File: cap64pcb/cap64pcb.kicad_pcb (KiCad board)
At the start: 2 copper layers, 91.6 x 8 mm, 29 parts, among them J1 SM05B_SURS_TF, Q1 BSS138, Q2 BSS138, U1 MPR121QR2, U2 SPX3819M5-L-3-3

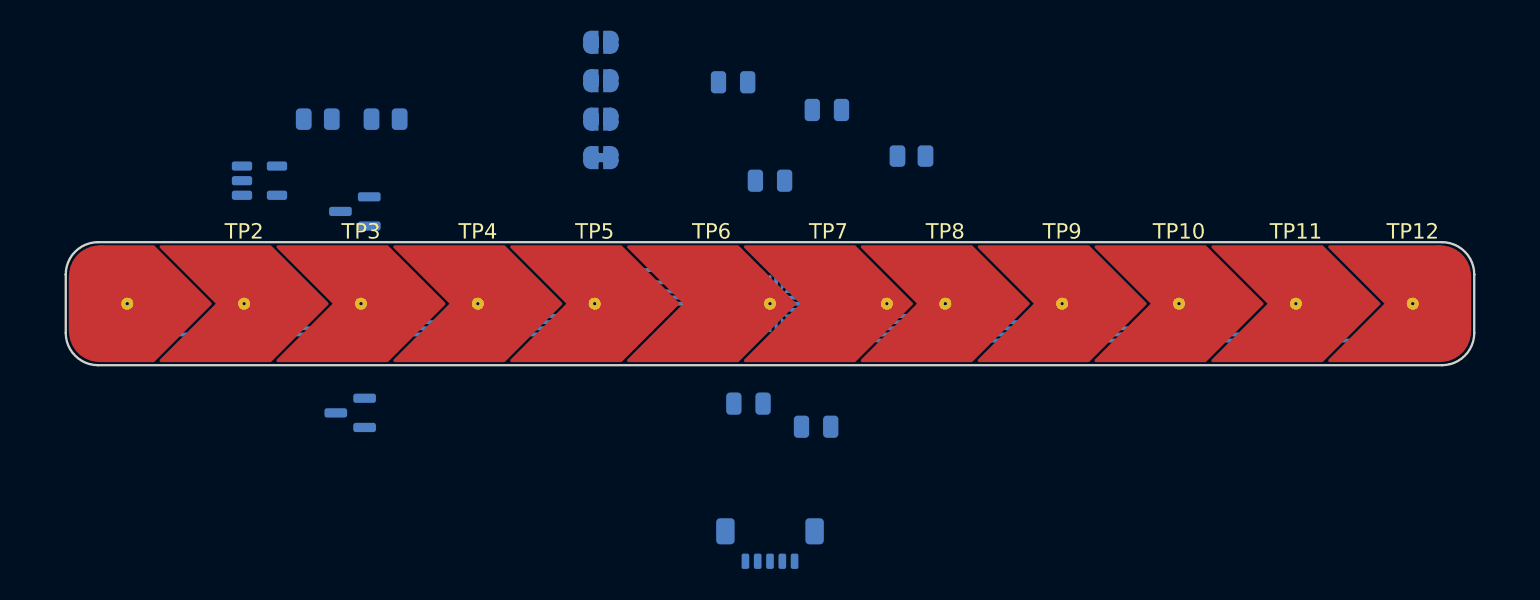
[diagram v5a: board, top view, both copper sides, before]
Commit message: shifted PTH up on touch pads
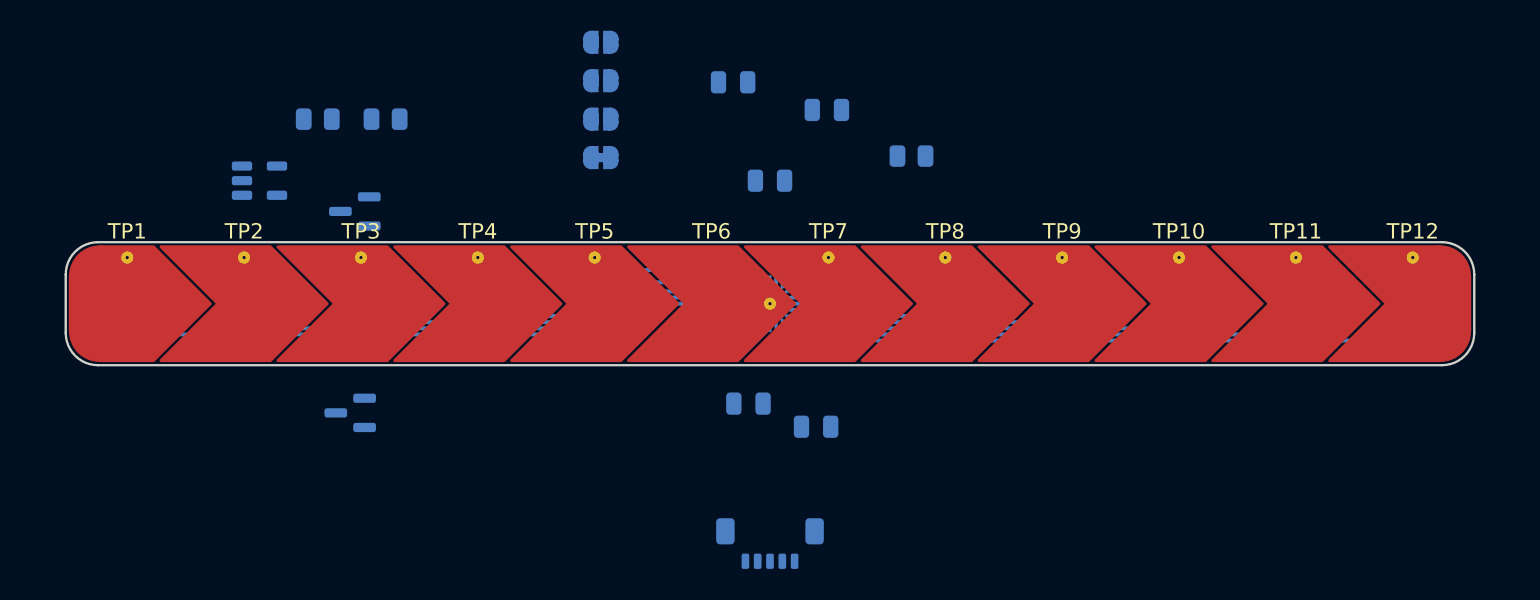
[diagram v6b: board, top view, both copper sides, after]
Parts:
- TP1: footprint cap_pads:CAPPAD_7.6x7.6_Chevron_1 -> cap_pads:CAPPAD_7.6x7.6_Chevron_1_TopPTH
- TP10, TP11, TP2, TP3, TP4, TP5, TP8, TP9: footprint cap_pads:CAPPAD_7.6x7.6_Chevron_2 -> cap_pads:CAPPAD_7.6x7.6_Chevron_2_TopPTH
- TP12: footprint cap_pads:CAPPAD_7.6x7.6_Chevron_3 -> cap_pads:CAPPAD_7.6x7.6_Chevron_3_TopPTH
- TP7: footprint cap_pads:CAPPAD_7.6x7.6_Chevron_2_shifted -> cap_pads:CAPPAD_7.6x7.6_Chevron_2_TopPTH

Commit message: rerouted pads
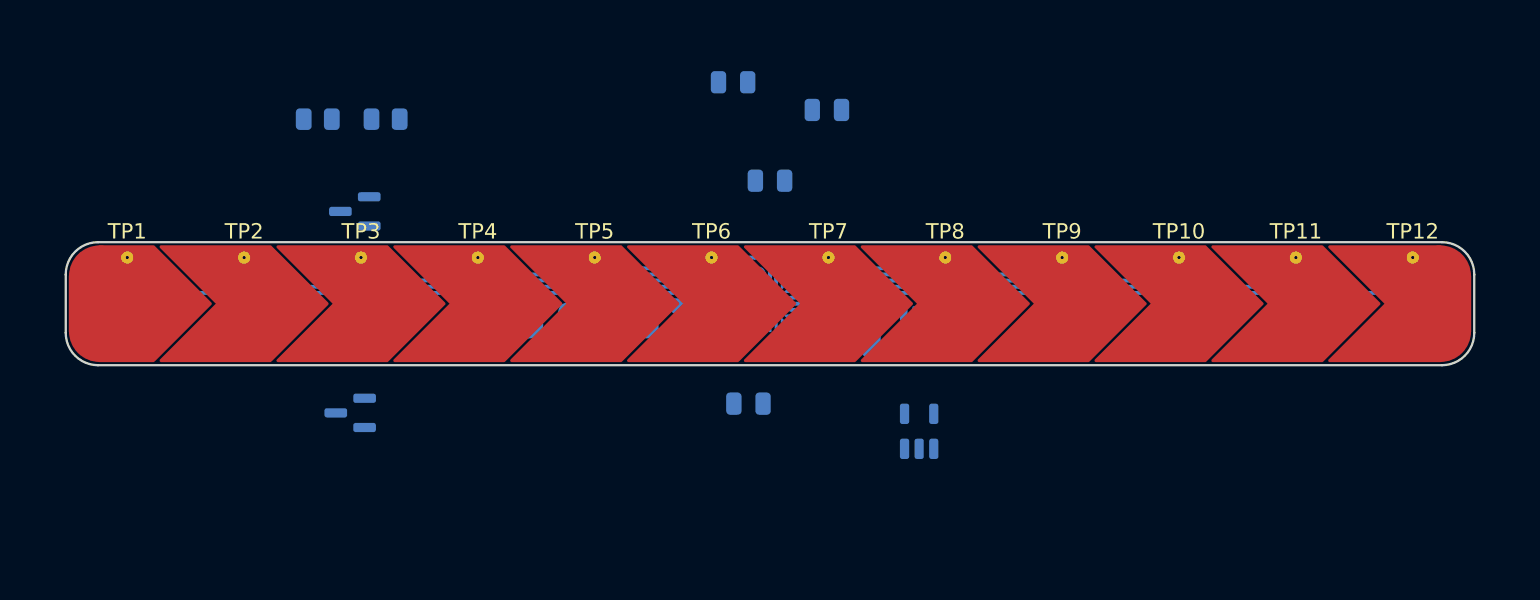
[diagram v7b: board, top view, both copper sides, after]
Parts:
- TP6: footprint cap_pads:CAPPAD_7.6x7.6_Chevron_2_shifted -> cap_pads:CAPPAD_7.6x7.6_Chevron_2_TopPTH
- moved U2 45.9 mm to (89.7, 53.3), turned to 90 degrees
- moved JP1 18.1 mm to (69.5, 46.1), turned to 90 degrees
- moved R1 16.8 mm to (76.3, 46.1), turned to -90 degrees
- moved J1 16.8 mm to (89.5, 46.8), turned to 180 degrees
- moved JP2 15.7 mm to (67.0, 46.1), turned to 90 degrees
- moved JP3 13.9 mm to (64.5, 46.1), turned to 90 degrees
- moved C5 11.1 mm to (74.3, 46.1), turned to 90 degrees
- moved JP4 11.0 mm to (72.0, 46.1), turned to -90 degrees
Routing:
- net Net-(U1-Pad14): track 8.60 -> 4.54 mm
- net Net-(U1-Pad13): track 1.39 -> 4.94 mm
- net Net-(U1-Pad7): track 0.00 -> 2.40 mm
- net Net-(U1-Pad19): track 42.0 -> 43.2 mm
- net Net-(U1-Pad8): track 41.9 -> 43.0 mm
- net Net-(U1-Pad18): track 34.3 -> 35.2 mm
- net Net-(U1-Pad9): track 34.1 -> 35.0 mm
- net Net-(U1-Pad17): track 26.5 -> 27.2 mm
- net Net-(U1-Pad10): track 26.4 -> 27.0 mm

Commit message: cleaning silks
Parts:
- moved U2 4.70 mm to (85.0, 53.1)
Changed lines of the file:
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@@
       (effects (font (size 1 1) (thickness 0.15)) (justify mirror))
     )
-    (fp_text value "GND" (at -3.5 0 90) (layer "B.SilkS")
+    (fp_text value "GND" (at -3.1 0 90) (layer "B.SilkS")
       (effects (font (size 1 1) (thickness 0.15)) (justify mirror))
     )
@@
     (property "Sheetname" "")
     (attr smd)
-    (fp_text reference "R3" (at 0 1.65) (layer "B.SilkS")
-      (effects (font (size 1 1) (thickness 0.15)) (justify mirror))
-    )
-    (fp_text value "10kΩ" (at 0 -1.65) (layer "B.Fab")
+    (fp_text reference "R3" (at 0 1.65) (layer "B.Fab")
+      (effects (font (size 1 1) (thickness 0.15)) (justify mirror))
+    )
+    (fp_text value "10kΩ" (at 0 -1.65) (layer "B.SilkS")
       (effects (font (size 1 1) (thickness 0.15)) (justify mirror))
     )
@@
     (property "Sheetname" "")
     (attr smd)
-    (fp_text reference "U1" (at 0 2.8 90) (layer "B.SilkS")
-      (effects (font (size 1 1) (thickness 0.15)) (justify mirror))
-    )
-    (fp_text value "MPR121QR2" (at 0 -2.8 90) (layer "B.Fab")
+    (fp_text reference "U1" (at 0 2.8 90) (layer "B.Fab")
+      (effects (font (size 1 1) (thickness 0.15)) (justify mirror))
+    )
+    (fp_text value "MPR121QR2" (at 2.8 0) (layer "B.SilkS")
       (effects (font (size 1 1) (thickness 0.15)) (justify mirror))
     )
@@
   )
   (footprint "Package_TO_SOT_SMD:SOT-23-5" (layer "B.Cu")
-    (at 89.7 53.3 90)
+    (at 85 53.15 90)
     (descr "SOT, 5 Pin (https://www.jedec.org/sites/default/files/docs/Mo-178c.PDF variant AA), generated with kicad-footprint-generator ipc_gullwing_generator.py")
     (tags "SOT TO_SOT_SMD")
@@
       (effects (font (size 1 1) (thickness 0.15)) (justify mirror))
     )
-    (fp_text value "SPX3819M5-L-3-3" (at 0 -2.4 90) (layer "B.Fab")
+    (fp_text value "SPX3819M5-L-3-3" (at 0 -2.4 90) (layer "B.SilkS")
       (effects (font (size 1 1) (thickness 0.15)) (justify mirror))
     )
@@
       (effects (font (size 1 1) (thickness 0.15)) (justify mirror))
     )
-    (fp_text value "SDA" (at -3.5 0 90) (layer "B.SilkS")
+    (fp_text value "SDA" (at 3.05 0 90) (layer "B.SilkS")
       (effects (font (size 1 1) (thickness 0.15)) (justify mirror))
     )
@@
       (effects (font (size 1 1) (thickness 0.15)) (justify mirror))
     )
-    (fp_text value "3V3" (at -3.3 0 90) (layer "B.SilkS")
+    (fp_text value "3V3" (at 2.95 0 90) (layer "B.SilkS")
       (effects (font (size 1 1) (thickness 0.15)) (justify mirror))
     )
@@
       (effects (font (size 1 1) (thickness 0.15)) (justify mirror))
     )
-    (fp_text value "BSS138" (at 0 -2.4) (layer "B.Fab")
+    (fp_text value "BSS138" (at 0 -2.4) (layer "B.SilkS")
       (effects (font (size 1 1) (thickness 0.15)) (justify mirror))
     )
@@
     (property "Sheetname" "")
     (attr smd)
-    (fp_text reference "R2" (at 0 1.65) (layer "B.SilkS")
-      (effects (font (size 1 1) (thickness 0.15)) (justify mirror))
-    )
-    (fp_text value "10kΩ" (at 0 -1.65) (layer "B.Fab")
+    (fp_text reference "R2" (at 0 1.65) (layer "B.Fab")
+      (effects (font (size 1 1) (thickness 0.15)) (justify mirror))
+    )
+    (fp_text value "10kΩ" (at 0 -1.65) (layer "B.SilkS")
       (effects (font (size 1 1) (thickness 0.15)) (justify mirror))
     )
@@
       (effects (font (size 1 1) (thickness 0.15)) (justify mirror))
     )
-    (fp_text value "SCL" (at -3.5 0 90) (layer "B.SilkS")
-      (effects (font (size 1 1) (thickness 0.15)) (justify mirror))
-    )
+    (fp_text value "SCL" (at 3.05 0 90) (layer "B.SilkS")
+      (effects (font (size 1 1) (thickness 0.15)) (justify mirror))
+    )
